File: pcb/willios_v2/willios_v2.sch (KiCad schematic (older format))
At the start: 51 parts, among them J1 Screw_Terminal_01x02, J10 Conn_01x01_Female, J11 Conn_01x01_Female, J12 Conn_01x01_Female, J2 USB_B_Micro, J3 SWD, J4 Conn_01x04_Female, J5 Conn_01x04_Female, J6 Conn_01x06_Female, J7 Conn_01x01_Female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

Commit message: Layout willios_v2
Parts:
- removed C14: 12p, symbol Device:C_Small
- added C13: 12p, Capacitor_SMD:C_0402_1005Metric, symbol Device:C_Small
- added H1, H2, H3, H4: MountingHole_Pad, MountingHole:MountingHole_3.2mm_M3_Pad_Via, symbol Mechanical:MountingHole_Pad
- C1, C5: footprint (none) -> Capacitor_SMD:C_0603_1608Metric
- C10, C11, C12, C6, C7, C8, C9: footprint (none) -> Capacitor_SMD:C_0402_1005Metric
- C14: renamed from C13; footprint (none) -> Capacitor_SMD:C_0402_1005Metric
- C2: footprint (none) -> Capacitor_SMD:C_1206_3216Metric
- C3, C4: value 10n -> 10u; footprint (none) -> Capacitor_SMD:C_1206_3216Metric
- D1, D2: footprint (none) -> Diode_SMD:D_SOD-123
- D3, D4: footprint (none) -> LED_SMD:LED_0603_1608Metric
- F1: footprint (none) -> Fuse:Fuse_1206_3216Metric
- FB1: footprint (none) -> Inductor_SMD:L_0805_2012Metric
- J1: footprint (none) -> TerminalBlock_Phoenix:TerminalBlock_Phoenix_PT-1,5-2-3.5-H_1x02_P3.50mm_Horizontal
- J10, J11, J12, J7: footprint (none) -> Connector_PinSocket_2.54mm:PinSocket_1x01_P2.54mm_Vertical
- J2: footprint (none) -> Connector_USB:USB_Micro-B_Molex_47346-0001
- J3: footprint (none) -> Connector_PinSocket_2.54mm:PinSocket_2x05_P2.54mm_Vertical
- J4, J5: footprint (none) -> Connector_PinSocket_2.54mm:PinSocket_1x04_P2.54mm_Vertical
- J6: footprint (none) -> Connector_PinSocket_2.54mm:PinSocket_1x06_P2.54mm_Vertical
- J8: footprint (none) -> Connector_PinSocket_2.54mm:PinSocket_1x03_P2.54mm_Vertical
- J9: footprint (none) -> Connector_PinSocket_2.54mm:PinSocket_1x05_P2.54mm_Vertical
- L1: footprint (none) -> Inductor_SMD:L_Sunlord_MWSA0518_5.4x5.2mm
- L2: footprint (none) -> Inductor_SMD:L_0402_1005Metric
- R1, R11, R2, R3, R4, R5, R6, R7, R8: footprint (none) -> Resistor_SMD:R_0603_1608Metric
- R10, R9: footprint (none) -> Resistor_SMD:R_0402_1005Metric
- SW1: footprint (none) -> Button_Switch_SMD:SW_SPDT_PCM12
- U1: footprint (none) -> Package_TO_SOT_SMD:SOT-23-6
- Y1: value 16MHz -> Crystal_GND24_Small; footprint (none) -> Crystal:Crystal_SMD_3225-4Pin_3.2x2.5mm
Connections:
- net +3V3: no longer J1.1 (Pin_1)
- net +9V: now also J1.1 (Pin_1)
- net GND: now also C14.2, C13.2, H1.1, H2.1, H3.1, H4.1; no longer C14.1, R10.2, U3.5 (PH0)
- net HSE_IN: now reaches Y1.1
- net HSE_IN: now also U3.5 (PH0), C13.1; no longer C14.2
- net at Y1.3: now also C14.1, R10.2
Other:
- note added: "Holes"
- moved on the sheet: C14

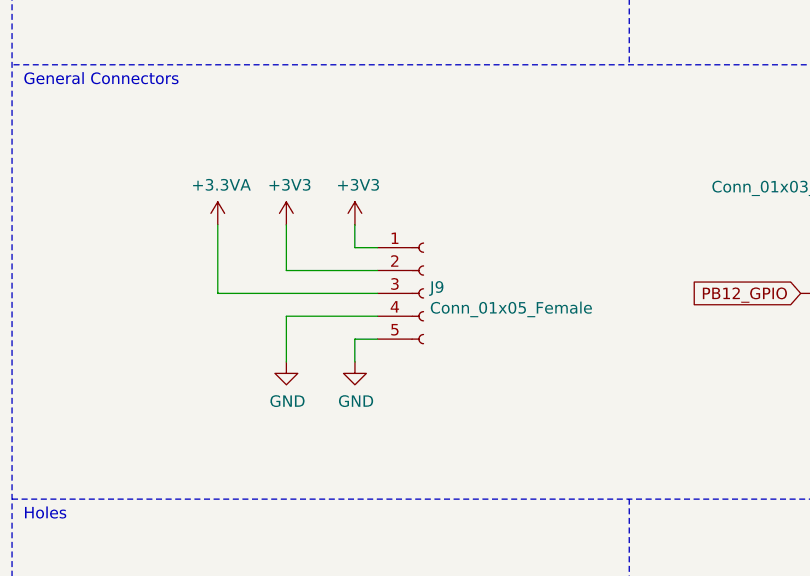
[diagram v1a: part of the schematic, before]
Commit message: Routing pre-oscillator
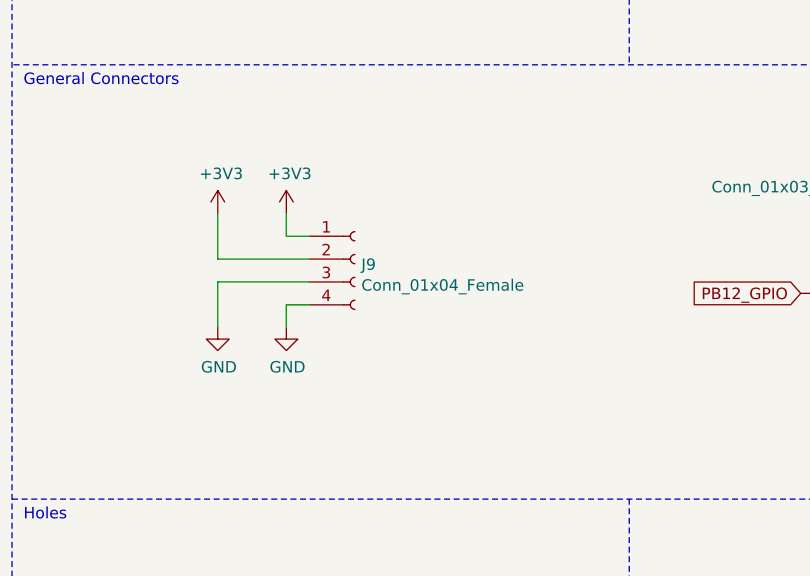
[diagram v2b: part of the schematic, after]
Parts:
- removed J9: Conn_01x05_Female, Connector_PinSocket_2.54mm:PinSocket_1x05_P2.54mm_Vertical, symbol Connector:Conn_01x05_Female
- added J9: Conn_01x04_Female, Connector_PinSocket_2.54mm:PinSocket_1x04_P2.54mm_Vertical, symbol Connector:Conn_01x04_Female
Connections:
- net +3V3: now also J9.1 (Pin_1), J9.2 (Pin_2)
- net GND: now also J9.3 (Pin_3), J9.4 (Pin_4)
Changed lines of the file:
@@
-$EndComp
-$Comp
-L Connector:Conn_01x05_Female J9
-U 1 1 60EB66A7
-P 10300 7350
-F 0 "J9" H 10328 7376 50  0000 L CNN
-F 1 "Conn_01x05_Female" H 10328 7285 50  0000 L CNN
-F 2 "Connector_PinSocket_2.54mm:PinSocket_1x05_P2.54mm_Vertical" H 10300 7350 50  0001 C CNN
-F 3 "~" H 10300 7350 50  0001 C CNN
-	1    10300 7350
-	1    0    0    -1
-$EndComp
-$Comp
-L power:+3V3 #PWR040
-U 1 1 60EB7994
-P 10000 7050
-F 0 "#PWR040" H 10000 6900 50  0001 C CNN
-F 1 "+3V3" H 10015 7223 50  0000 C CNN
-F 2 "" H 10000 7050 50  0001 C CNN
-F 3 "" H 10000 7050 50  0001 C CNN
-	1    10000 7050
-	1    0    0    -1
-$EndComp
-$Comp
-L power:+3V3 #PWR039
-U 1 1 60EB8E4C
-P 9700 7050
-F 0 "#PWR039" H 9700 6900 50  0001 C CNN
-F 1 "+3V3" H 9715 7223 50  0000 C CNN
-F 2 "" H 9700 7050 50  0001 C CNN
-F 3 "" H 9700 7050 50  0001 C CNN
-	1    9700 7050
-	1    0    0    -1
-$EndComp
-$Comp
-L power:+3.3VA #PWR038
-U 1 1 60EB9A38
-P 9400 7050
-F 0 "#PWR038" H 9400 6900 50  0001 C CNN
-F 1 "+3.3VA" H 9415 7223 50  0000 C CNN
-F 2 "" H 9400 7050 50  0001 C CNN
-F 3 "" H 9400 7050 50  0001 C CNN
-	1    9400 7050
-	1    0    0    -1
 $EndComp
 $Comp
 L power:GND #PWR043
 U 1 1 60EBB71A
-P 10000 7650
-F 0 "#PWR043" H 10000 7400 50  0001 C CNN
-F 1 "GND" H 10005 7477 50  0000 C CNN
-F 2 "" H 10000 7650 50  0001 C CNN
-F 3 "" H 10000 7650 50  0001 C CNN
-	1    10000 7650
+P 9700 7500
+F 0 "#PWR043" H 9700 7250 50  0001 C CNN
+F 1 "GND" H 9705 7327 50  0000 C CNN
+F 2 "" H 9700 7500 50  0001 C CNN
+F 3 "" H 9700 7500 50  0001 C CNN
+	1    9700 7500
 	1    0    0    -1
 $EndComp
@@
 L power:GND #PWR042
 U 1 1 60EBC833
-P 9700 7650
-F 0 "#PWR042" H 9700 7400 50  0001 C CNN
-F 1 "GND" H 9705 7477 50  0000 C CNN
-F 2 "" H 9700 7650 50  0001 C CNN
-F 3 "" H 9700 7650 50  0001 C CNN
-	1    9700 7650
-	1    0    0    -1
-$EndComp
-Wire Wire Line
-	10000 7050 10000 7150
-Wire Wire Line
-	10000 7150 10100 7150
-Wire Wire Line
-	9700 7050 9700 7250
-Wire Wire Line
-	9700 7250 10100 7250
-Wire Wire Line
-	10100 7350 9400 7350
-Wire Wire Line
-	9400 7350 9400 7050
-Wire Wire Line
-	10100 7550 10000 7550
-Wire Wire Line
-	10000 7550 10000 7650
-Wire Wire Line
-	10100 7450 9700 7450
-Wire Wire Line
-	9700 7450 9700 7650
+P 9400 7500
+F 0 "#PWR042" H 9400 7250 50  0001 C CNN
+F 1 "GND" H 9405 7327 50  0000 C CNN
+F 2 "" H 9400 7500 50  0001 C CNN
+F 3 "" H 9400 7500 50  0001 C CNN
+	1    9400 7500
+	1    0    0    -1
+$EndComp
 $Comp
 L Connector:Conn_01x01_Female J12
@@
 	-1   0    0    1
 $EndComp
-Text GLabel 11950 7350 0    50   Input ~ 0
-PB12_GPIO
 $Comp
 L Connector:Conn_01x01_Female J10
@@
 	1    0    0    -1
 $EndComp
+$Comp
+L power:+3V3 #PWR0101
+U 1 1 61C20A0C
+P 9400 7000
+F 0 "#PWR0101" H 9400 6850 50  0001 C CNN
+F 1 "+3V3" H 9415 7173 50  0000 C CNN
+F 2 "" H 9400 7000 50  0001 C CNN
+F 3 "" H 9400 7000 50  0001 C CNN
+	1    9400 7000
+	1    0    0    -1
+$EndComp
+$Comp
+L power:+3V3 #PWR0102
+U 1 1 61C18A34
+P 9700 7000
+F 0 "#PWR0102" H 9700 6850 50  0001 C CNN
+F 1 "+3V3" H 9715 7173 50  0000 C CNN
+F 2 "" H 9700 7000 50  0001 C CNN
+F 3 "" H 9700 7000 50  0001 C CNN
+	1    9700 7000
+	1    0    0    -1
+$EndComp
+$Comp
+L Connector:Conn_01x04_Female J9
+U 1 1 61C16E46
+P 10000 7200
+F 0 "J9" H 10028 7176 50  0000 L CNN
+F 1 "Conn_01x04_Female" H 10028 7085 50  0000 L CNN
+F 2 "Connector_PinSocket_2.54mm:PinSocket_1x04_P2.54mm_Vertical" H 10000 7200 50  0001 C CNN
+F 3 "~" H 10000 7200 50  0001 C CNN
+	1    10000 7200
+	1    0    0    -1
+$EndComp
+Text GLabel 11950 7350 0    50   Input ~ 0
+PB12_GPIO
+Wire Wire Line
+	9800 7100 9700 7100
+Wire Wire Line
+	9700 7100 9700 7000
+Wire Wire Line
+	9800 7200 9400 7200
+Wire Wire Line
+	9400 7200 9400 7000
+Wire Wire Line
+	9800 7400 9700 7400
+Wire Wire Line
+	9700 7400 9700 7500
+Wire Wire Line
+	9800 7300 9400 7300
+Wire Wire Line
+	9400 7300 9400 7500
 $EndSCHEMATC
